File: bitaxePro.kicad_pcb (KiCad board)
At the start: 4 copper layers, 59.5 x 61.2 mm, 103 parts, among them IC1 BM1387, IC2 BM1387, IC3 TCR2EF18, IC4 TCR2EF18, J1 Conn_01x01, J2 Conn_01x01, J3 Conn_01x05, J4 Conn_01x02, J5 Conn_01x03, Y1 25MHz

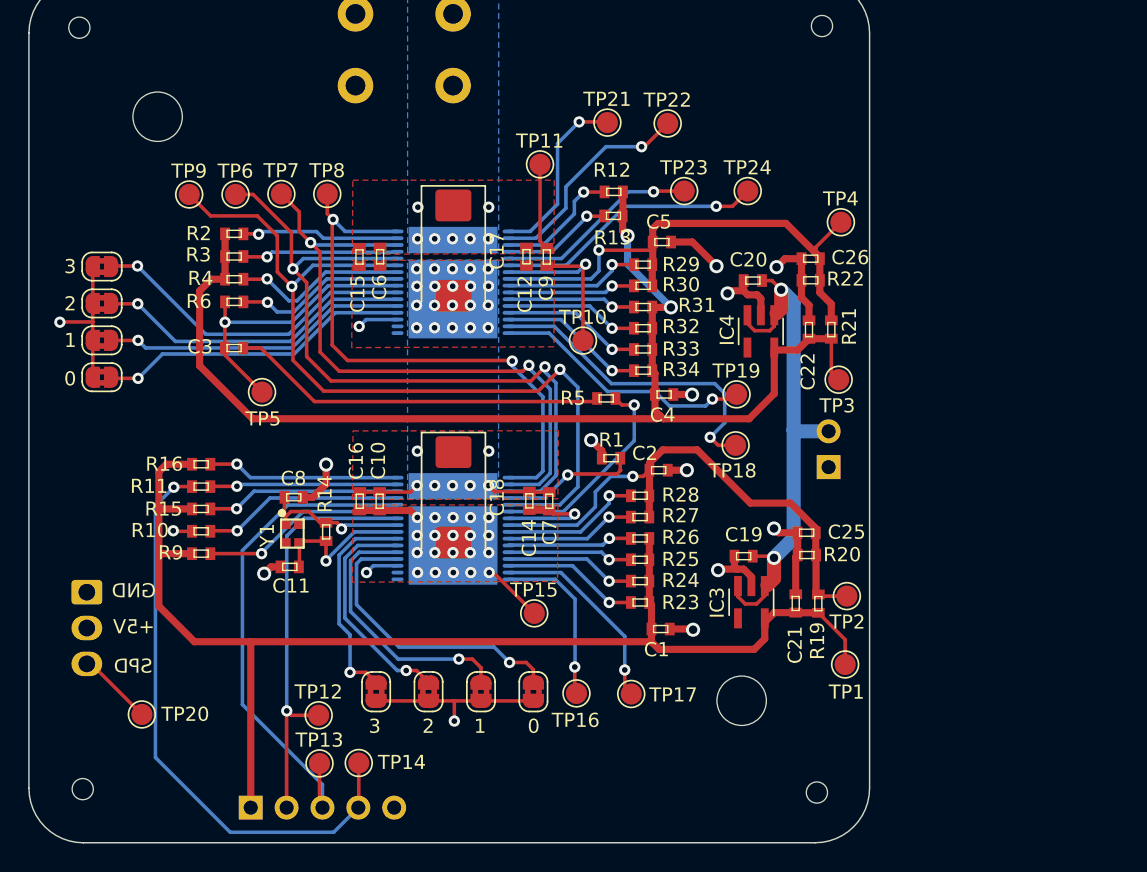
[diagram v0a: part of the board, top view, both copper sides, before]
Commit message: made separate symbols for BM1397 in mode0 and mode1
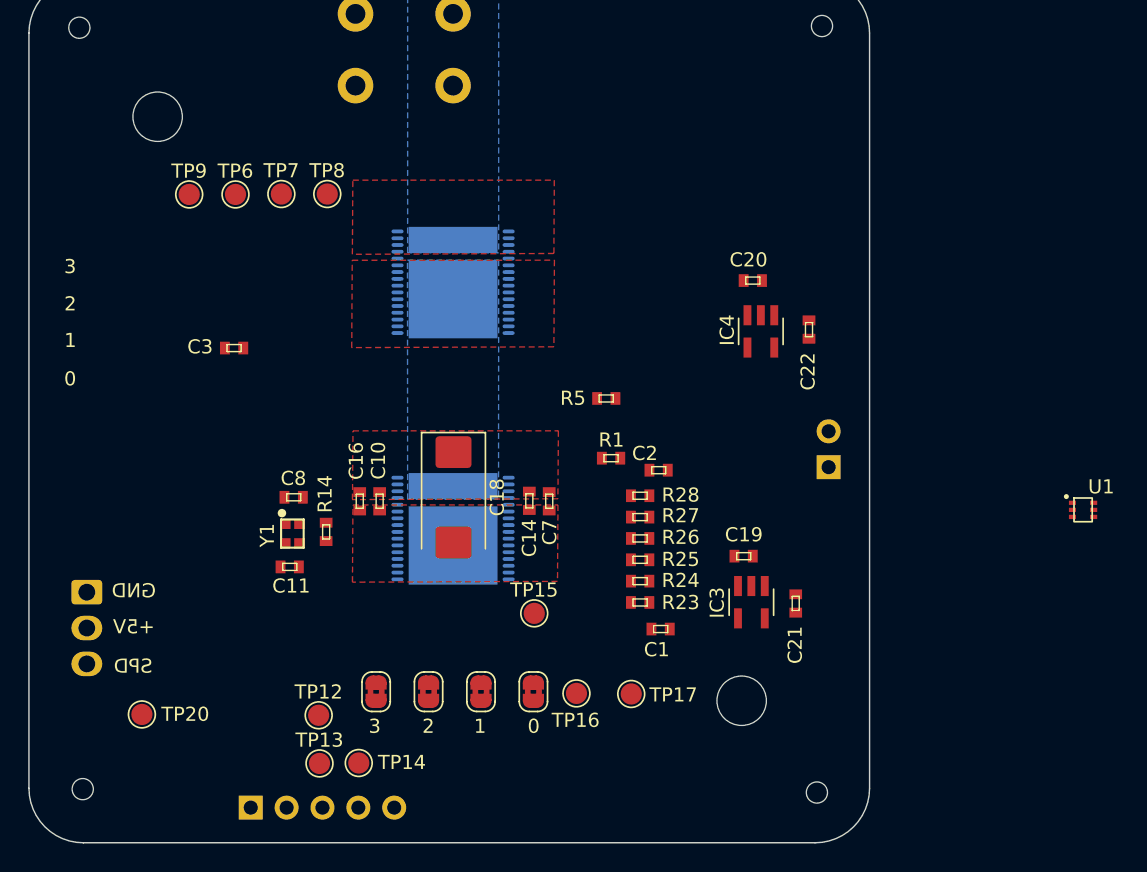
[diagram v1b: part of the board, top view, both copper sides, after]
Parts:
- removed C12, C15: 587-5514-1-ND, DayMiner:C0402
- removed C17: 330uF, Capacitor_Tantalum_SMD:CP_EIA-7343-31_Kemet-D_Pad2.25x2.55mm_HandSolder
- removed C25, C26, C6, C9: 311-3342-1-ND, DayMiner:C0402
- removed C4, C5: 1uF, DayMiner:C0402
- removed JP1, JP2, JP3, JP4: SolderJumper_2_Bridged, Jumper:SolderJumper-2_P1.3mm_Bridged2Bar_RoundedPad1.0x1.5mm
- removed R10, R11, R12, R13, R15, R16, R2, R3, R4, R9: 10k, DayMiner:R0402
- removed R19, R20, R21, R22: 100, DayMiner:R0402
- removed R29, R30, R31, R32, R33, R34: 0, DayMiner:R0402
- removed R6: 33, DayMiner:R0402
- removed TP1, TP10, TP11, TP18, TP19, TP2, TP21, TP22, TP23, TP24, TP3, TP4, TP5: TestPoint, TestPoint:TestPoint_Pad_D1.5mm
- removed kibuzzard-6222FC9E: G***, kibuzzard-6222FC9E
- removed kibuzzard-62A3C9C0: G***, kibuzzard-62A3C9C0
- added U1: SN74LVC1T45DRLR, DayMiner:SN74LVC1T45DRLR, F.Cu at (133.9, 83.8)
- added kibuzzard-62AD2371: G***, kibuzzard-62AD2371, B.Cu at (100.0, 104.1)
- IC4: value TCR2EF18 -> TCR2EF08
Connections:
- net /1V8_1 renamed /0V8
- C21 pad 1: /1V8_2 -> /1V8
- C3 pad 1: Net-(C3-Pad1) -> unconnected-(C3-Pad1)
- IC2 pad 1: Net-(IC1-Pad32) -> Net-(IC2-Pad1)
- IC2 pad 2: Net-(IC1-Pad30) -> Net-(IC2-Pad2)
- IC2 pad 27: Net-(IC2-Pad27) -> unconnected-(IC2-Pad27)
- IC2 pad 28: /RO -> unconnected-(IC2-Pad28)
- IC2 pad 29: Net-(IC2-Pad29) -> unconnected-(IC2-Pad29)
- IC2 pad 3: Net-(IC1-Pad28) -> Net-(IC2-Pad3)
- IC2 pad 30: Net-(IC2-Pad30) -> unconnected-(IC2-Pad30)
- IC2 pad 31: Net-(IC2-Pad31) -> unconnected-(IC2-Pad31)
- IC2 pad 32: Net-(IC2-Pad32) -> unconnected-(IC2-Pad32)
- IC2 pad 5: Net-(IC1-Pad27) -> Net-(IC2-Pad5)
- IC3 pad 5: /1V8_2 -> /1V8
- TP6 pad 1: Net-(IC1-Pad28) -> Net-(IC2-Pad3)
- TP7 pad 1: Net-(IC1-Pad30) -> Net-(IC2-Pad2)
- TP8 pad 1: Net-(IC1-Pad32) -> Net-(IC2-Pad1)
- TP9 pad 1: Net-(IC1-Pad27) -> Net-(IC2-Pad5)
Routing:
- net /1V8_2: track 90.2 -> 0.00 mm
- net /5V: track 88.3 -> 0.00 mm, vias 2 -> 0
- net /0V8: track 83.3 -> 0.00 mm, vias 2 -> 0
- net Net-(IC1-Pad27): track 59.6 -> 0.00 mm, vias 2 -> 0
- net GND: track 52.9 -> 0.00 mm, vias 31 -> 0
- net /A: track 52.1 -> 0.00 mm, vias 34 -> 0
- net Net-(IC1-Pad28): track 51.9 -> 0.00 mm, vias 2 -> 0
- net Net-(IC1-Pad30): track 45.6 -> 0.00 mm, vias 2 -> 0
- net /RST_N: track 41.4 -> 0.00 mm, vias 1 -> 0
- net Net-(IC1-Pad32): track 40.4 -> 0.00 mm, vias 2 -> 0
- net /0V8_2: track 37.3 -> 0.00 mm, vias 1 -> 0
- net /0V8_1: track 36.7 -> 0.00 mm, vias 1 -> 0
- net /RO: track 36.1 -> 0.00 mm
- net /CI: track 30.0 -> 0.00 mm, vias 1 -> 0
- net Net-(C3-Pad2): track 26.7 -> 0.00 mm
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
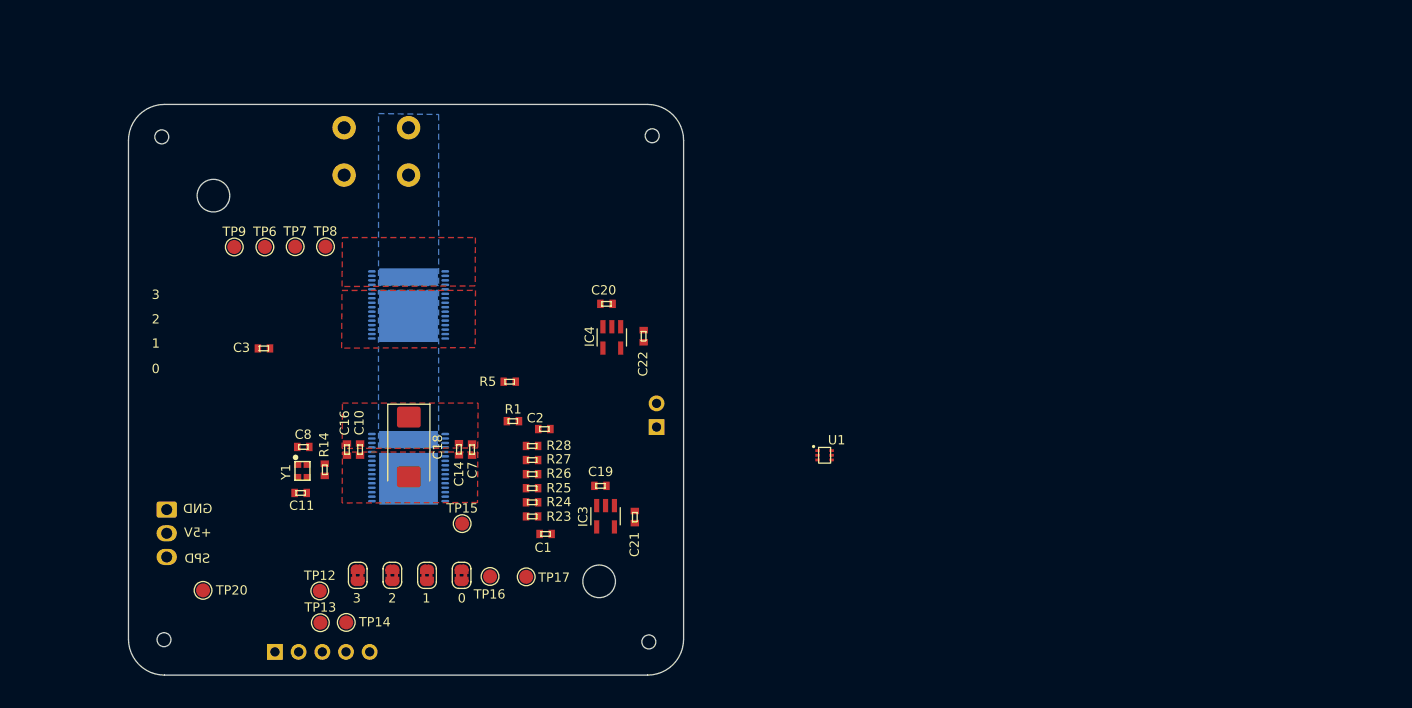
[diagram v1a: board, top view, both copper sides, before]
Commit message: added an ESP32-C3 to try out. Added a NCT218
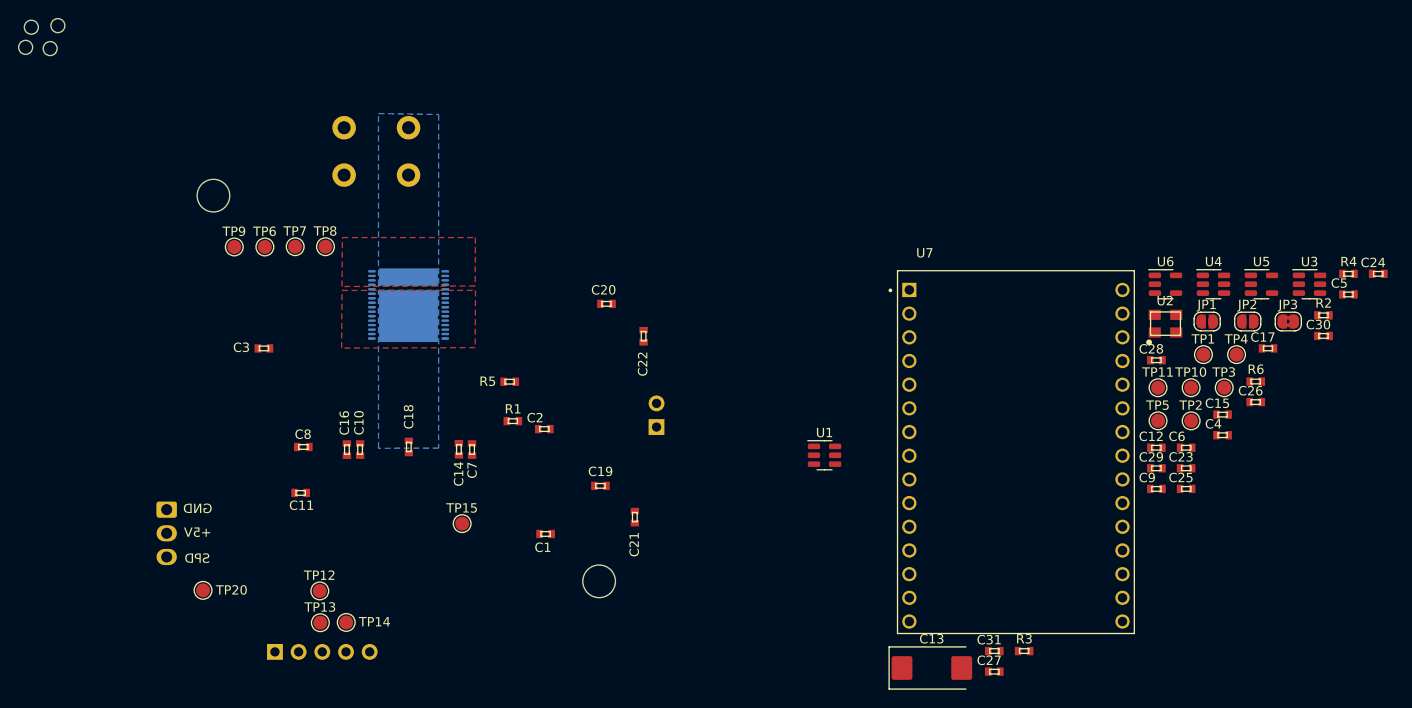
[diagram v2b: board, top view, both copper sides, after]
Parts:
- removed IC2: BM1387, DayMiner:SON45P800X800X70-33T645X800N
- removed IC3: TCR2EF18, DayMiner:TCR2EF18
- removed IC4: TCR2EF08, DayMiner:TCR2EF18
- removed JP5, JP6, JP7, JP8: SolderJumper_2_Bridged, Jumper:SolderJumper-2_P1.3mm_Bridged2Bar_RoundedPad1.0x1.5mm
- removed R14: 311-1.00MLRCT-ND, DayMiner:R0402
- removed R23, R24, R25, R26, R27, R28: 0, DayMiner:R0402
- removed TP16, TP17: TestPoint, TestPoint:TestPoint_Pad_D1.5mm
- removed Y1: 25MHz, DayMiner:XRCGB25M000F2P02R0
- added C12: 587-5514-1-ND, DayMiner:C0402, F.Cu at (169.5, 83.0)
- added C13: 330uF, Capacitor_Tantalum_SMD:CP_EIA-7343-31_Kemet-D_Pad2.25x2.55mm_HandSolder, F.Cu at (145.4, 106.6)
- added C15: 587-5514-1-ND, DayMiner:C0402, F.Cu at (176.6, 79.4)
- added C17: 587-5514-1-ND, DayMiner:C0402, F.Cu at (181.5, 72.3)
- added C23: 311-3342-1-ND, DayMiner:C0402, F.Cu at (172.7, 85.2)
- added C24: 311-3342-1-ND, DayMiner:C0402, F.Cu at (193.3, 64.3)
- added C25: 311-3342-1-ND, DayMiner:C0402, F.Cu at (172.7, 87.4)
- added C26: 311-3342-1-ND, DayMiner:C0402, F.Cu at (180.2, 78.1)
- added C27: 311-3342-1-ND, DayMiner:C0402, F.Cu at (152.1, 107.0)
- added C28: 311-3342-1-ND, DayMiner:C0402, F.Cu at (169.5, 73.6)
- added C29: 587-5514-1-ND, DayMiner:C0402, F.Cu at (169.5, 85.2)
- added C30: 587-5514-1-ND, DayMiner:C0402, F.Cu at (187.4, 71.0)
- added C31: 587-5514-1-ND, DayMiner:C0402, F.Cu at (152.1, 104.8)
- added C4: 587-5514-1-ND, DayMiner:C0402, F.Cu at (176.6, 81.6)
- added C5: 587-5514-1-ND, DayMiner:C0402, F.Cu at (190.1, 66.5)
- added C6: 587-5514-1-ND, DayMiner:C0402, F.Cu at (172.7, 83.0)
- added C9: 311-3342-1-ND, DayMiner:C0402, F.Cu at (169.5, 87.4)
- added JP1: SolderJumper_2_Open, Jumper:SolderJumper-2_P1.3mm_Open_RoundedPad1.0x1.5mm, F.Cu at (174.9, 69.4)
- added JP2: SolderJumper_2_Open, Jumper:SolderJumper-2_P1.3mm_Open_RoundedPad1.0x1.5mm, F.Cu at (179.3, 69.4)
- added JP3: SolderJumper_2_Bridged, Jumper:SolderJumper-2_P1.3mm_Bridged2Bar_RoundedPad1.0x1.5mm, F.Cu at (183.6, 69.4)
- added R2: 33, DayMiner:R0402, F.Cu at (187.4, 68.8)
- added R3: 0, DayMiner:R0402, F.Cu at (155.3, 104.8)
- added R4: 0, DayMiner:R0402, F.Cu at (190.1, 64.3)
- added R6: 10k, DayMiner:R0402, F.Cu at (180.2, 75.9)
- added TP1: TestPoint, TestPoint:TestPoint_Pad_D1.5mm, F.Cu at (174.5, 73.0)
- added TP10: TestPoint, TestPoint:TestPoint_Pad_D1.5mm, F.Cu at (173.2, 76.5)
- added TP11: TestPoint, TestPoint:TestPoint_Pad_D1.5mm, F.Cu at (169.7, 76.5)
- added TP2: TestPoint, TestPoint:TestPoint_Pad_D1.5mm, F.Cu at (173.2, 80.1)
- added TP3: TestPoint, TestPoint:TestPoint_Pad_D1.5mm, F.Cu at (176.8, 76.5)
- added TP4: TestPoint, TestPoint:TestPoint_Pad_D1.5mm, F.Cu at (178.1, 73.0)
- added TP5: TestPoint, TestPoint:TestPoint_Pad_D1.5mm, F.Cu at (169.7, 80.1)
- added U2: oscillator, DayMiner:O 25,0-JO32-B-1V3-1-T1-LF, F.Cu at (170.5, 69.7)
- added U3: SN74LVC1T45DRLR, Package_TO_SOT_SMD:SOT-23-6, F.Cu at (185.9, 65.4)
- added U4: SN74LVC1T45DRLR, Package_TO_SOT_SMD:SOT-23-6, F.Cu at (175.6, 65.4)
- added U5: MCP1824, Package_TO_SOT_SMD:SOT-23-5, F.Cu at (180.8, 65.4)
- added U6: MCP1824, Package_TO_SOT_SMD:SOT-23-5, F.Cu at (170.5, 65.4)
- added U7: ESP32-C3-DEVKITC-02, DayMiner:XCVR_ESP32-C3-DEVKITC-02, F.Cu at (154.4, 83.4)
- C1: value 1uF -> 311-3342-1-ND
- C10: value 311-3342-1-ND -> 587-5514-1-ND
- C11, C8: value 311-3607-1-ND -> 587-5514-1-ND
- C18: value 330uF -> 587-5514-1-ND; footprint Capacitor_Tantalum_SMD:CP_EIA-7343-31_Kemet-D_Pad2.25x2.55mm_HandSolder -> DayMiner:C0402
- C2: value 1uF -> 587-5514-1-ND
- C3: value 0.1uF -> 587-5514-1-ND
- IC1: value BM1387 -> BM1397_mode1
- R1: value 10k -> 470
- R5: value 33 -> 1K
- U1: footprint DayMiner:SN74LVC1T45DRLR -> Package_TO_SOT_SMD:SOT-23-6
- moved H4 92.4 mm to (48.2, 40.0)
- moved H3 67.6 mm to (48.8, 37.9)
- moved H6 66.8 mm to (51.7, 37.7)
- moved H5 15.3 mm to (50.9, 40.1)
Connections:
- net /CI renamed /TX
- C1 pad 1: /1V8_2 -> GND
- C1 pad 2: GND -> /1V8
- C10 pad 1: /A -> /VDD
- C11 pad 1: Net-(C11-Pad1) -> /VDD
- C14 pad 1: /A -> /1V8
- C16 pad 1: /A -> /0V8
- C18 pad 1: /A -> Net-(C17-Pad2)
- C2 pad 1: /0V8_2 -> GND
- C2 pad 2: GND -> Net-(C2-Pad2)
- C20 pad 2: /A -> GND
- C22 pad 2: /A -> GND
- C3 pad 1: unconnected-(C3-Pad1) -> Net-(C2-Pad2)
- C7 pad 1: /A -> /VDD
- C8 pad 1: Net-(C8-Pad1) -> Net-(C6-Pad2)
- C8 pad 2: GND -> /VDD
- IC1 pad 1: Net-(IC1-Pad1) -> Net-(C6-Pad2)
- IC1 pad 13: Net-(IC1-Pad13) -> GND
- IC1 pad 14: Net-(IC1-Pad14) -> /0V8
- IC1 pad 15: Net-(IC1-Pad15) -> /0V8
- IC1 pad 16: Net-(IC1-Pad16) -> /1V8
- IC1 pad 17: unconnected-(IC1-Pad17) -> /1V8
- IC1 pad 18: unconnected-(IC1-Pad18) -> /0V8
- IC1 pad 19: /A -> GND
- IC1 pad 2: Net-(IC1-Pad2) -> Net-(C3-Pad2)
- IC1 pad 23: Net-(IC1-Pad23) -> unconnected-(IC1-Pad23)
- IC1 pad 24: Net-(C3-Pad1) -> unconnected-(IC1-Pad24)
- IC1 pad 3: Net-(IC1-Pad3) -> Net-(C2-Pad2)
- IC1 pad 30: Net-(IC1-Pad30) -> Net-(C17-Pad2)
- IC1 pad 33: /VIN -> /VDD
- IC1 pad 34: /A -> GND
- IC1 pad 7: /A -> unconnected-(IC1-Pad7)
- IC1 pad 8: /0V8_1 -> Net-(IC1-Pad8)
- IC1 pad 9: Net-(IC1-Pad9) -> /RST_N
- J1 pad 1: /VIN -> /VDD
- J3 pad 1: /1V8_2 -> /VCCIO
- J3 pad 3: /RO -> /RX
- J3 pad 4: /RST_N -> /RST
- R1 pad 2: Net-(IC2-Pad4) -> Net-(IC1-Pad8)
- R5 pad 1: Net-(C3-Pad2) -> GND
- R5 pad 2: Net-(IC2-Pad6) -> /RST_N
- TP13 pad 1: /RO -> /RX
- TP14 pad 1: /RST_N -> /RST
- TP6 pad 1: Net-(IC2-Pad3) -> Net-(IC1-Pad25)
- TP7 pad 1: Net-(IC2-Pad2) -> Net-(IC1-Pad22)
- TP8 pad 1: Net-(IC2-Pad1) -> Net-(IC1-Pad21)
- TP9 pad 1: Net-(IC2-Pad5) -> Net-(IC1-Pad20)
- U1 pad 1: unconnected-(U1-Pad1) -> /VCCIO
- U1 pad 2: unconnected-(U1-Pad2) -> GND
- U1 pad 3: unconnected-(U1-Pad3) -> /RX
- U1 pad 4: unconnected-(U1-Pad4) -> /RO
- U1 pad 5: unconnected-(U1-Pad5) -> GND
- U1 pad 6: unconnected-(U1-Pad6) -> /1V8
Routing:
- added copper zone on B.Cu, net /VDD
- added copper zone on F.Cu, net /VDD
- added copper zone on B.Cu, net GND
- removed copper zone on B.Cu, net /A
- removed copper zone on F.Cu, net /A
- removed copper zone on In2.Cu, net /A
- removed copper zone on B.Cu, net /VIN
- removed copper zone on F.Cu, net /VIN
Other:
- board outline removed
- board text removed: "0"
- board text removed: "1"
- board text removed: "2"
- board text removed: "3"

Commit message: lots of routing
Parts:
- removed kibuzzard-62AD2371: G***, kibuzzard-62AD2371
- added C32: 1000pF, DayMiner:C0402, F.Cu at (78.0, 79.0)
- added C33: 311-3342-1-ND, DayMiner:C0402, F.Cu at (74.2, 81.0)
- added R10: 1K, DayMiner:R0402, F.Cu at (112.5, 59.3)
- added R11: 1K, DayMiner:R0402, F.Cu at (112.5, 61.9)
- added R7: 10K, DayMiner:R0402, F.Cu at (139.2, 89.8)
- added R8: 100, Resistor_SMD:R_0402_1005Metric, F.Cu at (77.5, 77.6)
- added R9: 100, Resistor_SMD:R_0402_1005Metric, F.Cu at (78.6, 80.6)
- added TP16: TestPoint, TestPoint:TestPoint_Pad_D1.5mm, F.Cu at (127.3, 69.5)
- added TP17: TestPoint, TestPoint:TestPoint_Pad_D1.5mm, F.Cu at (127.3, 66.8)
- added TP18: TestPoint, TestPoint:TestPoint_Pad_D1.5mm, F.Cu at (127.2, 74.6)
- added TP19: TestPoint, TestPoint:TestPoint_Pad_D1.5mm, F.Cu at (143.1, 66.9)
- added TP21: TestPoint, TestPoint:TestPoint_Pad_D1.5mm, F.Cu at (127.2, 86.5)
- added TP22: TestPoint, TestPoint:TestPoint_Pad_D1.5mm, F.Cu at (127.5, 92.8)
- added TP23: TestPoint, TestPoint:TestPoint_Pad_D1.5mm, F.Cu at (144.7, 87.3)
- added U8: NCT218, Package_DFN_QFN:DFN-8_2x2mm_P0.5mm, F.Cu at (74.1, 78.9)
- added kibuzzard-62B6C053: G***, kibuzzard-62B6C053, B.Cu at (123.0, 51.0)
- U7: moved to B.Cu
- moved U5 109.4 mm to (74.2, 90.3)
- moved TP4 105.3 mm to (72.8, 71.6)
- moved TP3 104.3 mm to (72.8, 68.4)
- moved C17 101.2 mm to (80.3, 68.7), turned to 180 degrees
- moved TP5 99.9 mm to (69.9, 75.0)
- moved R6 99.3 mm to (81.1, 82.3), turned to -90 degrees
- moved C15 95.8 mm to (81.6, 67.0), turned to 180 degrees
- moved C5 95.6 mm to (95.8, 82.3), turned to 90 degrees
- moved R4 92.8 mm to (98.8, 81.1), turned to 180 degrees
- moved TP10 92.8 mm to (81.3, 88.8)
- moved R2 89.7 mm to (98.8, 82.6), turned to 180 degrees
- moved C12 88.4 mm to (82.9, 65.2), turned to 180 degrees
- moved U6 88.4 mm to (85.9, 91.2)
- moved C4 82.3 mm to (94.3, 82.3), turned to 90 degrees
- moved C24 81.9 mm to (112.9, 80.3), turned to -90 degrees
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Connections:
- net Net-(IC1-Pad21) renamed /TEMP_N
- net Net-(IC1-Pad22) renamed /TEMP_P
- J3 pad 2: /TX -> /CI
- J3 pad 3: /RX -> /RO
- J3 pad 4: /RST -> /RST_N
- J5 pad 3: /PWM -> /FAN_TACH
- TP12 pad 1: /TX -> /CI
- TP13 pad 1: /RX -> /RO
- TP14 pad 1: /RST -> /RST_N
- TP20 pad 1: /PWM -> /FAN_TACH
- U7 pad 12: unconnected-(U7-Pad12) -> /TEMP_ALRT
- U7 pad 18: unconnected-(U7-Pad18) -> /SDA
- U7 pad 19: unconnected-(U7-Pad19) -> /SCL
- U7 pad 24: unconnected-(U7-Pad24) -> /RST
- U7 pad 26: unconnected-(U7-Pad26) -> /TX
- U7 pad 27: unconnected-(U7-Pad27) -> /RX
- U7 pad 4: unconnected-(U7-Pad4) -> Net-(U7-Pad4)
- U7 pad 6: unconnected-(U7-Pad6) -> /FAN_TACH
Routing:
- net /SCL: track 0.00 -> 121.3 mm, vias 0 -> 1
- net /5V: track 0.00 -> 120.9 mm, vias 0 -> 4
- net /SDA: track 0.00 -> 115.2 mm
- net /TEMP_ALRT: track 0.00 -> 113.9 mm, vias 0 -> 1
- net /1V8: track 0.00 -> 111.3 mm, vias 0 -> 6
- net /FAN_TACH: track 0.00 -> 96.6 mm, vias 0 -> 1
- net /RST_N: track 0.00 -> 61.9 mm, vias 0 -> 3
- net GND: track 0.00 -> 60.6 mm, vias 0 -> 19
- net /RO: track 0.00 -> 51.0 mm, vias 0 -> 2
- net /CI: track 0.00 -> 49.3 mm, vias 0 -> 2
- net /0V8: track 0.00 -> 45.9 mm, vias 0 -> 4
- net /TX: track 0.00 -> 25.3 mm
- net /RX: track 0.00 -> 21.5 mm
- net /VCCIO: track 0.00 -> 19.6 mm, vias 0 -> 7
- net Net-(IC1-Pad25): track 0.00 -> 18.4 mm, vias 0 -> 1
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- added copper zone on In2.Cu, net /VCCIO
- removed copper zone on B.Cu, net GND
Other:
- board outline added: 87.7 x 62.9 mm
- board text added: "TAC"
- board text added: "VIO"
- board text removed: "1V8"
- board text removed: "SPD"
